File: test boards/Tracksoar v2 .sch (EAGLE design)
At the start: 59 parts, among them IC1 BME280, J1 battery, Y1 16MHZ

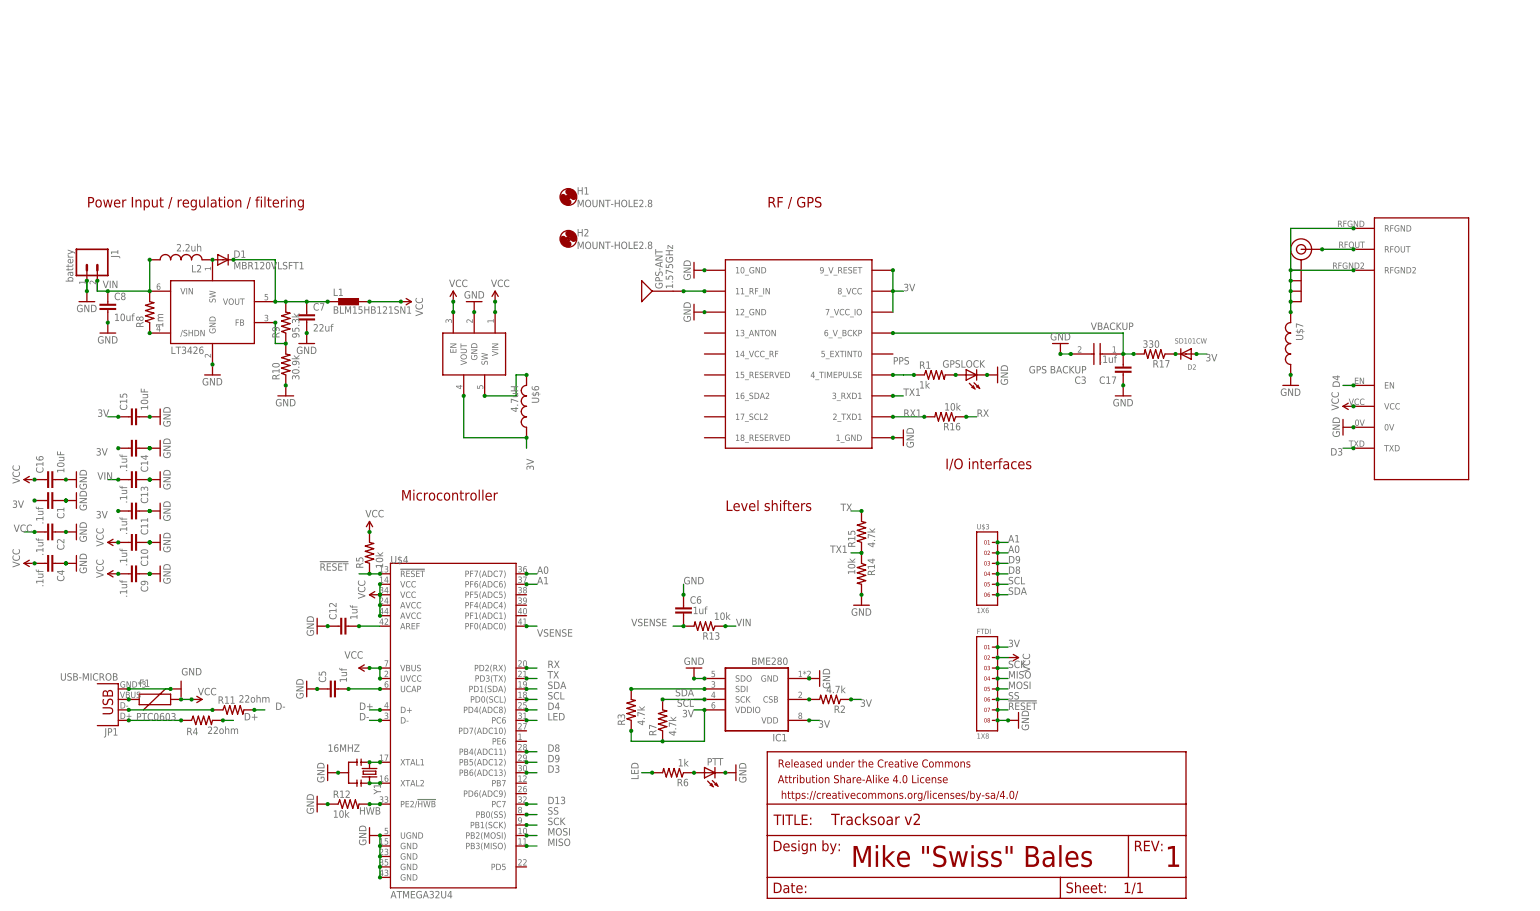
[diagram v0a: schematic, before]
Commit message: Schematic cleanup
placed decoupling caps where they are located on the board. Placed items in groups and did my best to place nets near their origins. Also generally group items where they are located on the board.
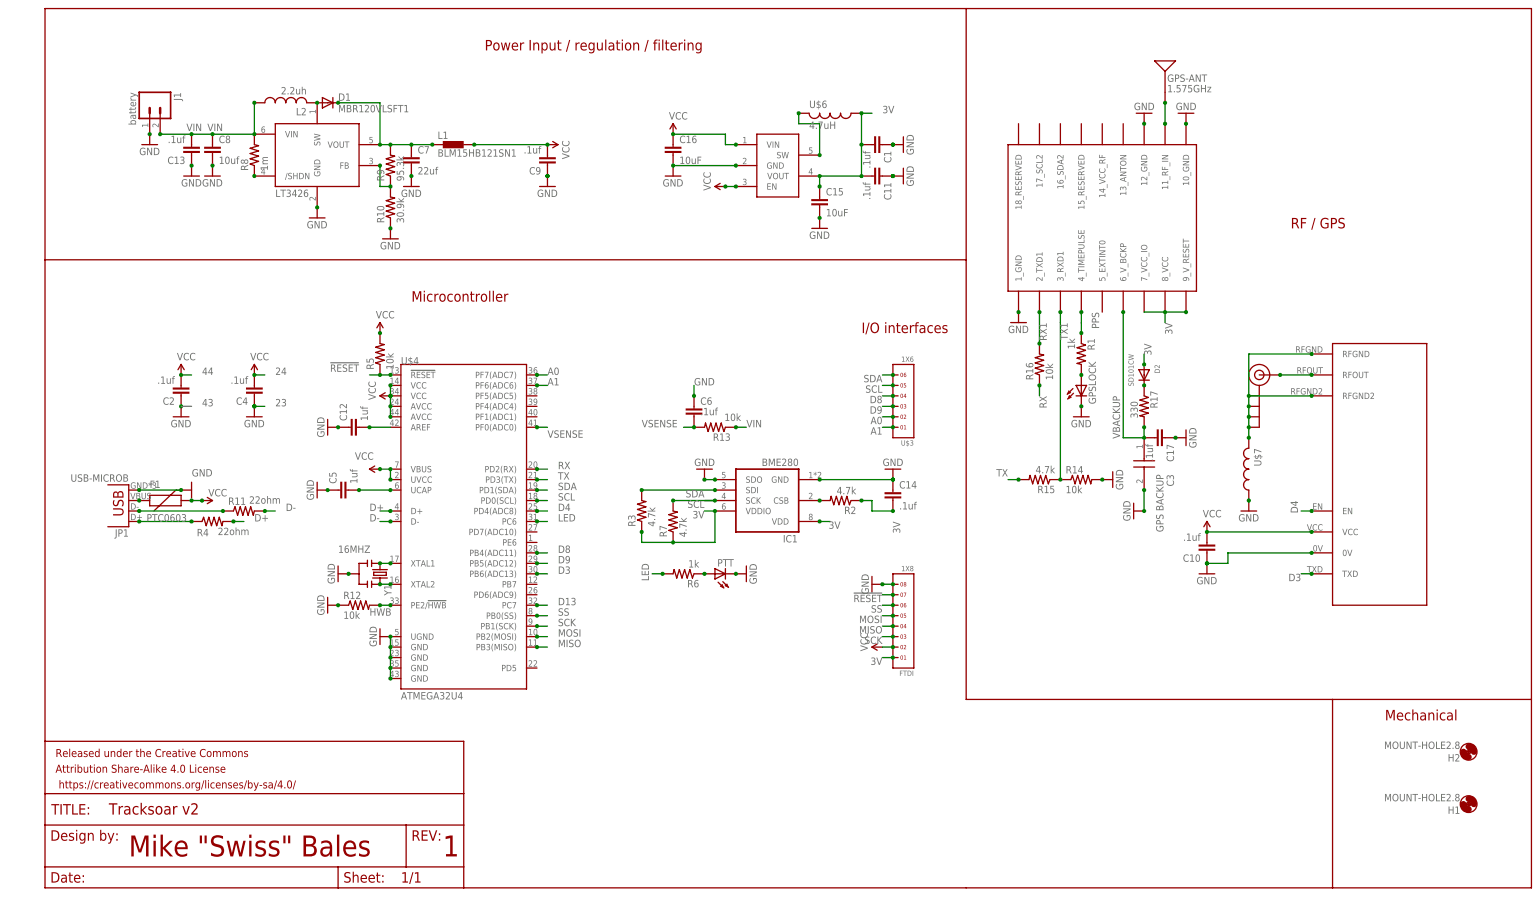
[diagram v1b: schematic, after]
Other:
- note added: "23"
- note added: "24"
- note added: "43"
- note added: "44"
- note added: "Mechanical"
- note removed: "Level shifters"
- moved on the sheet: C1, C10, C11, C12, C13, C14, C15, C16, C17, C2, C3, C4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

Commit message: Updated U$7
updated u$7 on brd and sch file to include value and part number
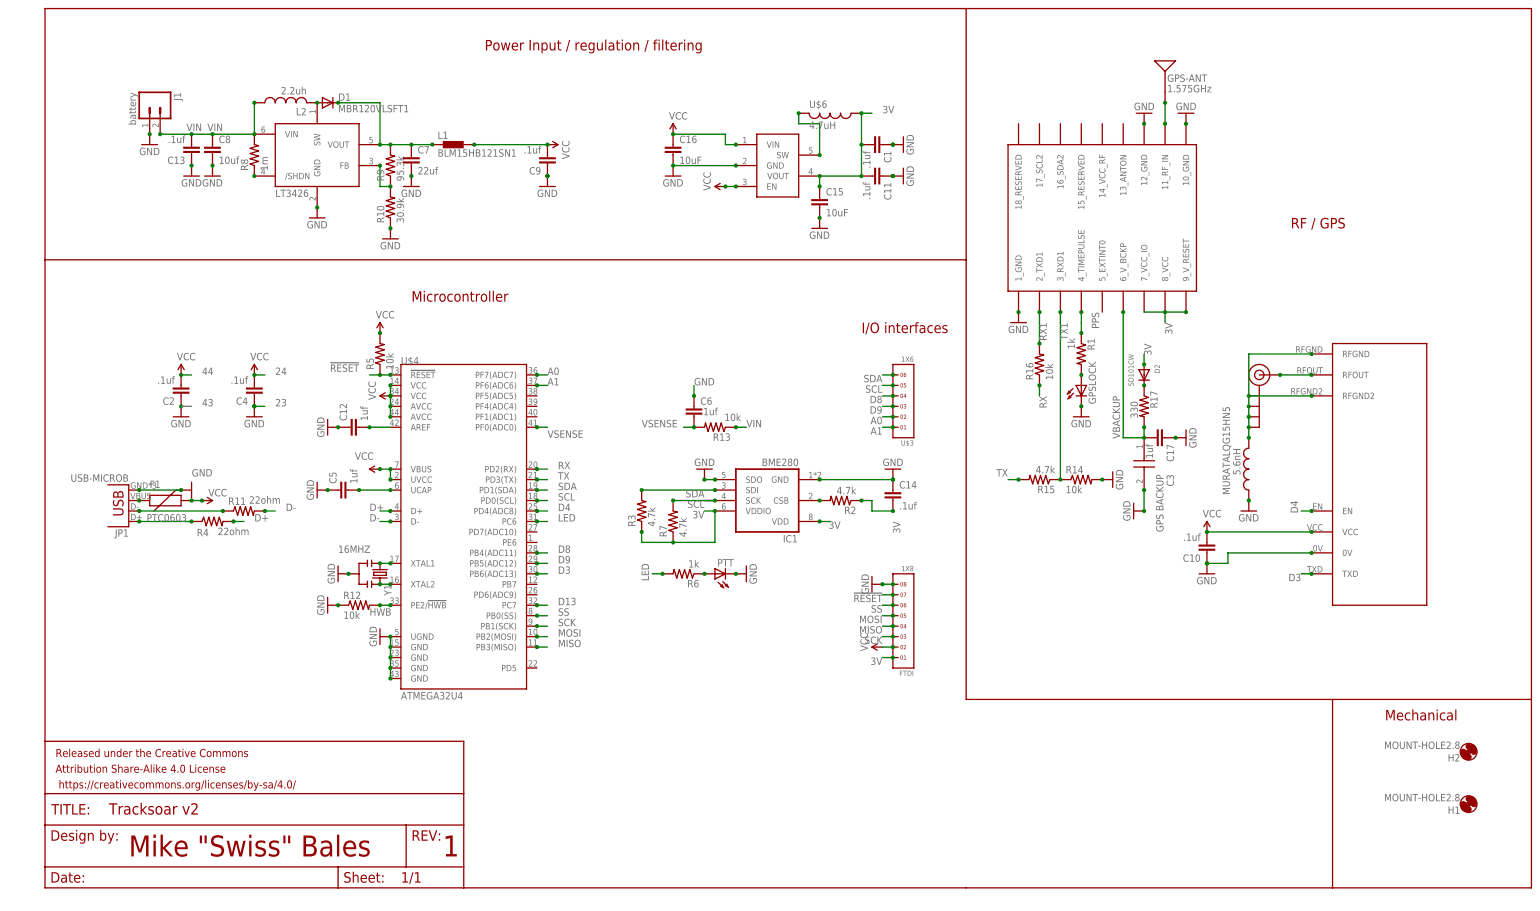
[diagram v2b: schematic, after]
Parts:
- MURATALQG15HN5: value (none) -> 5.6nH
- renumbered U$7 to MURATALQG15HN5
